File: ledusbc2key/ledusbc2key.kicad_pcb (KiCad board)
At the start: 2 copper layers, 43.8 x 54.3 mm, 28 parts, among them SW1 SW_Push, U1 ATmega32U2-A, U2 PRTR5V0U2X, Y1 Crystal_GND24_Small

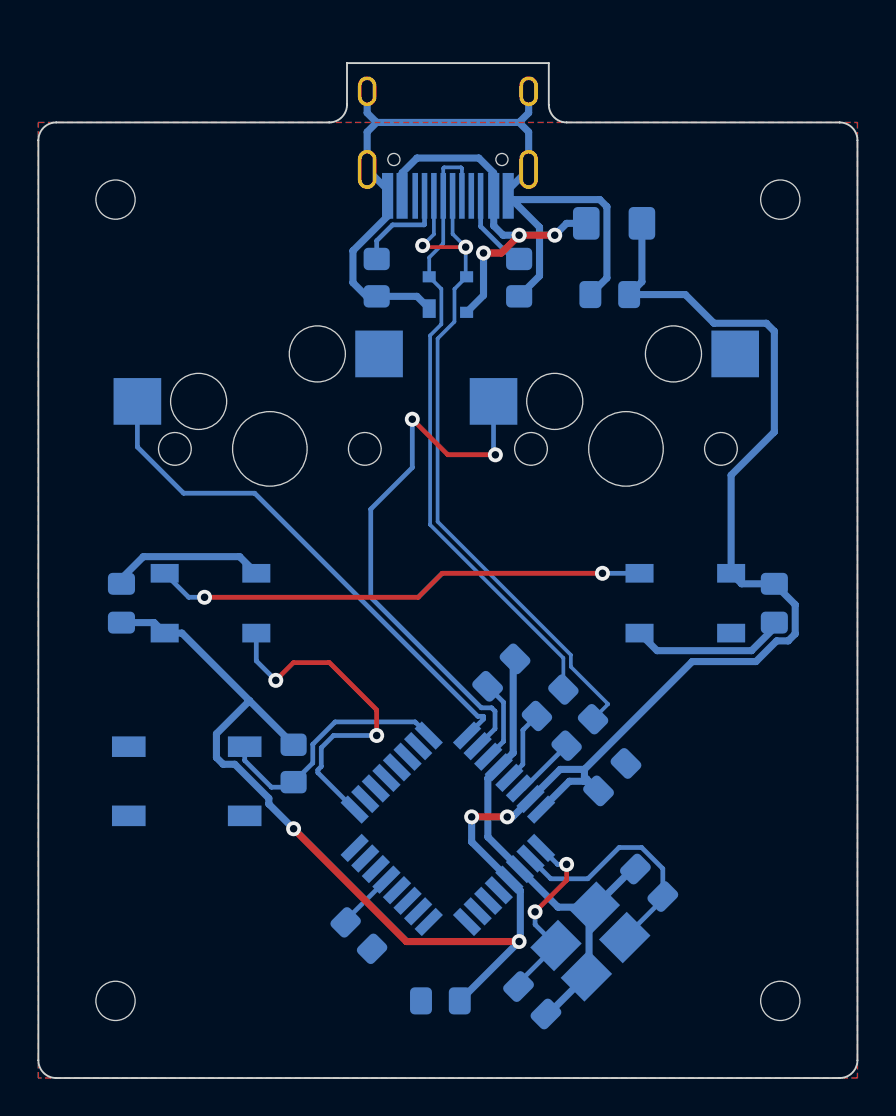
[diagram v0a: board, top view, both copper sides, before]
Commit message: swapped to new library for ledusbc
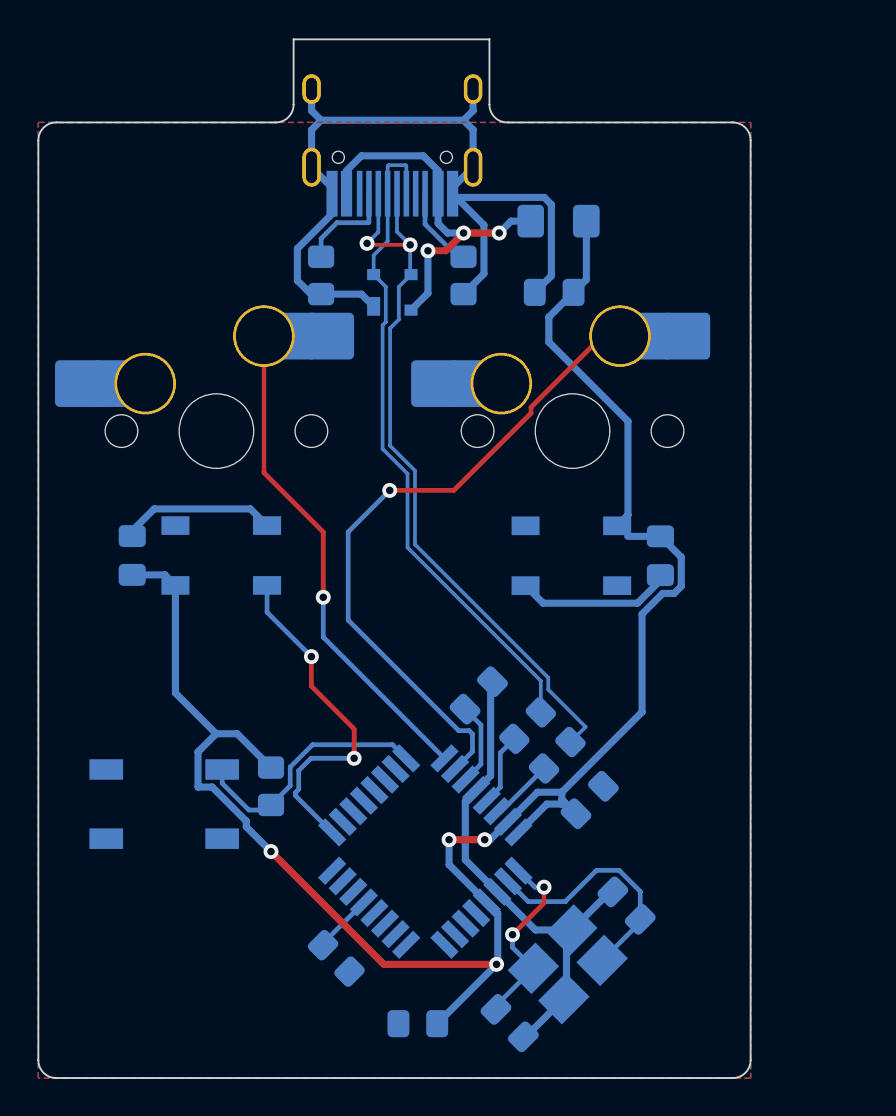
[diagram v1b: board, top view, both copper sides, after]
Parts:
- removed MX1, MX2: MX-NoLED, MX_Only:MXOnly-1U-Hotswap
- removed REF** (x4): MountingHole_2.1mm, MountingHole:MountingHole_2.1mm
- added SW2: MX_SW_HS, marbastlib-mx:SW_MX_HS_1u, B.Cu at (134.3, 78.4)
- added SW3: MX_SW_HS, marbastlib-mx:SW_MX_HS_1u, B.Cu at (115.3, 78.4)
- moved D2 6.60 mm to (134.2, 85.1)
- moved C4 6.60 mm to (139.0, 85.1)
- moved U2 2.97 mm to (124.7, 71.0)
- moved USB1 2.97 mm to (124.7, 57.5)
- moved C6 2.97 mm to (133.3, 71.0)
- moved F1 2.97 mm to (133.6, 67.2)
- moved R4 2.97 mm to (120.9, 70.1)
- moved R5 2.97 mm to (128.5, 70.1)
- moved C5 2.62 mm to (110.7, 85.1)
- moved D1 2.62 mm to (115.5, 85.1)
- moved C7 1.72 mm to (126.0, 110.1)
- moved R6 1.72 mm to (121.7, 106.6)
- moved SW1 1.72 mm to (112.5, 98.4)
- moved U1 1.72 mm to (126.4, 100.9)
- moved C1 1.72 mm to (129.3, 92.6)
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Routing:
- net Net-(D1-Pad2): track 26.5 -> 0.00 mm, vias 2 -> 0
- net +5V: track 106.6 -> 100.4 mm
- net COL0: track 30.0 -> 35.2 mm, vias 2 -> 1
- net COL1: track 28.3 -> 26.6 mm, vias 0 -> 1
- net D+: track 34.2 -> 35.9 mm
- net D-: track 38.3 -> 40.0 mm
- net GND: track 91.8 -> 91.2 mm
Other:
- board size 43.8 x 54.3 mm -> 38.1 x 55.6 mm

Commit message: did a bit of work 3d modelling today
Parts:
- moved C1 1.22 mm to (129.2, 91.3)
- moved C2 1.22 mm to (130.9, 108.9)
- moved C3 1.22 mm to (137.2, 102.6)
- moved C8 1.22 mm to (135.2, 96.9)
- moved R1 1.22 mm to (118.1, 96.2)
- moved R2 1.22 mm to (131.9, 93.0)
- moved R3 1.22 mm to (133.4, 94.5)
- moved SW1 1.22 mm to (112.4, 97.2)
- moved C7 1.22 mm to (126.0, 108.9)
- moved R6 1.22 mm to (121.6, 105.4)
- moved U1 1.22 mm to (126.4, 99.7)
- moved Y1 1.22 mm to (134.0, 105.7)
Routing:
- net +5V: track 100.4 -> 97.9 mm
- net D-: track 40.0 -> 39.5 mm
- net COL1: track 26.6 -> 26.0 mm
- net COL0: track 35.2 -> 34.7 mm
- net LED: track 18.6 -> 18.1 mm
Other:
- board size 38.1 x 55.6 mm -> 38.1 x 54.6 mm

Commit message: work
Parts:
- moved C2 12.0 mm to (138.8, 99.8), turned to -45 degrees
- moved R1 8.06 mm to (111.5, 91.6), turned to 0 degrees
- moved C3 5.84 mm to (132.5, 106.1), turned to 135 degrees
- moved Y1 3.20 mm to (135.7, 103.0), turned to -135 degrees
- moved C7 2.23 mm to (125.8, 106.7)
- moved R6 1.80 mm to (121.0, 103.7)
- moved U1 1.80 mm to (125.8, 98.0)
- moved R2 1.02 mm to (132.3, 92.1)
- moved R3 1.02 mm to (133.9, 93.6)
- moved C1 1.02 mm to (129.7, 90.4)
- moved C8 1.02 mm to (135.7, 96.0)
- moved SW1 0.16 mm to (112.5, 97.3), turned to -90 degrees
- moved USB1 0.12 mm to (124.8, 57.5)
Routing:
- net GND: track 91.2 -> 45.7 mm, vias 0 -> 2
- net Net-(D1-Pad2): track 0.00 -> 20.4 mm, vias 0 -> 2
- net +5V: track 97.9 -> 87.7 mm, vias 4 -> 2
- net COL0: track 34.7 -> 26.3 mm
- net LED: track 18.1 -> 11.5 mm
- net XTAL2: track 13.2 -> 7.95 mm
- net XTAL1: track 10.4 -> 14.4 mm, vias 2 -> 0
- net VCC: track 20.9 -> 24.3 mm, vias 3 -> 0
- net COL1: track 26.0 -> 23.4 mm
- net Net-(R1-Pad2): track 13.5 -> 15.5 mm
- net D-: track 39.5 -> 37.8 mm
- net Net-(C1-Pad1): track 4.46 -> 3.39 mm
- net D+: track 35.5 -> 36.3 mm, vias 0 -> 2
- net Net-(R3-Pad1): track 3.44 -> 4.17 mm
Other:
- board size 38.1 x 54.6 mm -> 38.1 x 52.2 mm
